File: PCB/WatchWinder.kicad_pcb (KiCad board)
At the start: 2 copper layers, 80 x 36.8 mm, 10 parts, among them J1 Screw_Terminal_01x02, J2 Screw_Terminal_01x02, J3 Screw_Terminal_01x12, J4 MOTOR, J5 Screw_Terminal_01x04

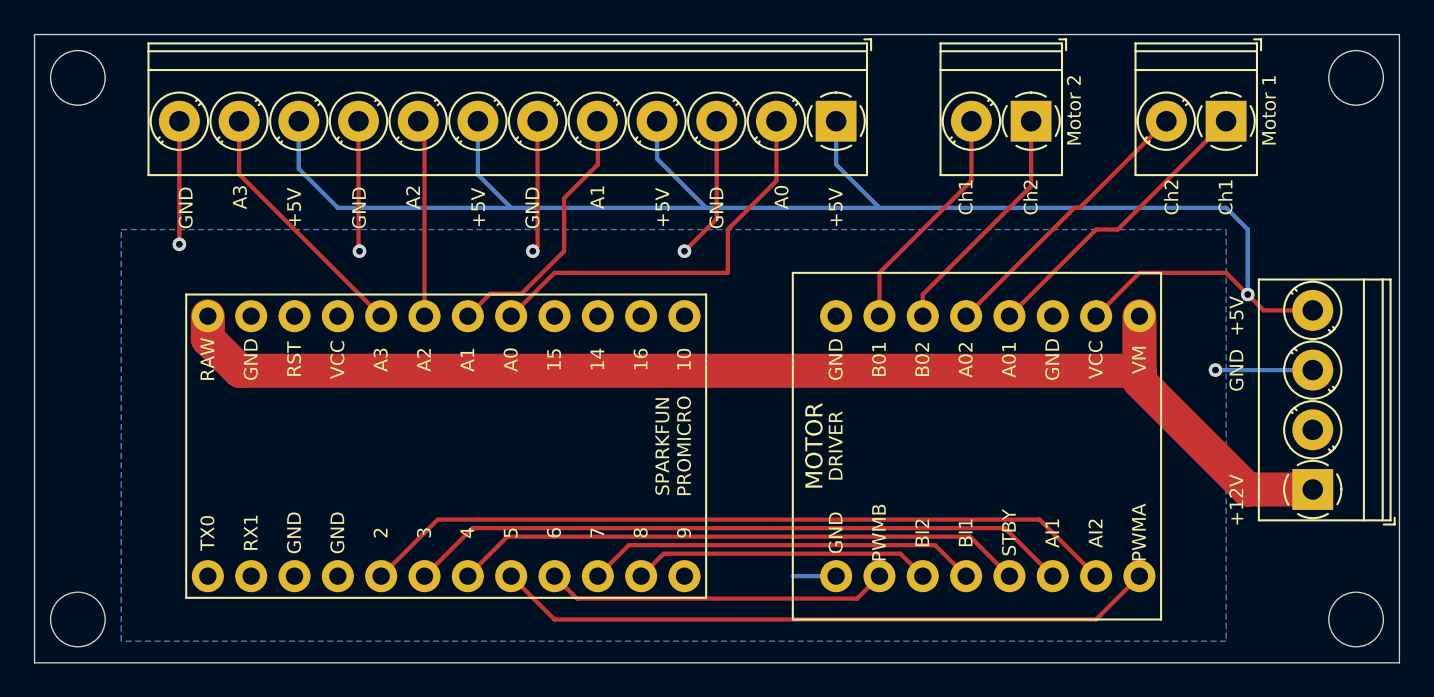
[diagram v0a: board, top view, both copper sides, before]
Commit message: Updated ground traces on PCB
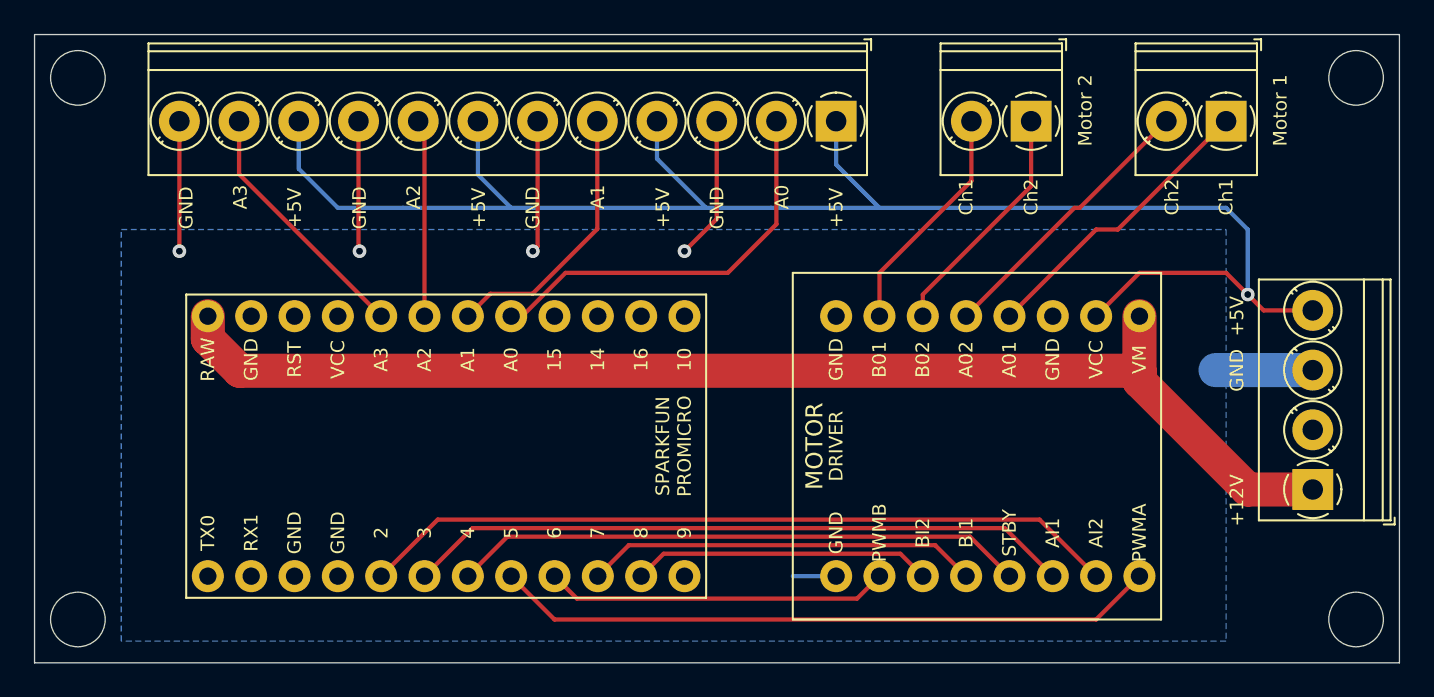
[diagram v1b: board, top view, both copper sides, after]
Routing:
- net GND: track 39.2 -> 39.6 mm, vias 5 -> 4
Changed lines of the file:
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@@
     (thickness 1.6)
     (drawings 29)
-    (tracks 93)
+    (tracks 91)
     (zones 0)
     (modules 10)
@@
   (setup
     (last_trace_width 0.25)
+    (user_trace_width 0.25)
+    (user_trace_width 2)
     (trace_clearance 0.25)
     (zone_clearance 0.508)
@@
     (effects (font (size 0.8 0.8) (thickness 0.15)))
   )
-  (gr_text "Motor 2" (at 135.89 76.835 90) (layer F.SilkS)
-    (effects (font (size 0.8 0.8) (thickness 0.15)))
-  )
-  (gr_text "Motor 1" (at 147.32 76.835 90) (layer F.SilkS)
+  (gr_text "Motor 2" (at 136.525 76.835 90) (layer F.SilkS)
+    (effects (font (size 0.8 0.8) (thickness 0.15)))
+  )
+  (gr_text "Motor 1" (at 147.955 76.835 90) (layer F.SilkS)
     (effects (font (size 0.8 0.8) (thickness 0.15)))
   )
@@
   (segment (start 149.86 99.06) (end 146.05 99.06) (width 2) (layer F.Cu) (net 1))
   (segment (start 121.92 104.14) (end 119.38 104.14) (width 0.25) (layer B.Cu) (net 2))
-  (segment (start 83.42 77.47) (end 83.42 84.69) (width 0.25) (layer F.Cu) (net 2))
-  (via (at 83.42 84.69) (size 0.8) (drill 0.4) (layers F.Cu B.Cu) (net 2))
   (via (at 93.98 85.09) (size 0.8) (drill 0.4) (layers F.Cu B.Cu) (net 2))
   (segment (start 93.92 85.03) (end 93.98 85.09) (width 0.25) (layer F.Cu) (net 2))
   (segment (start 93.92 77.47) (end 93.92 85.03) (width 0.25) (layer F.Cu) (net 2))
-  (via (at 104.14 85.09) (size 0.8) (drill 0.4) (layers F.Cu B.Cu) (net 2))
-  (segment (start 104.42 84.81) (end 104.14 85.09) (width 0.25) (layer F.Cu) (net 2))
-  (segment (start 104.42 77.47) (end 104.42 84.81) (width 0.25) (layer F.Cu) (net 2))
   (via (at 113.03 85.09) (size 0.8) (drill 0.4) (layers F.Cu B.Cu) (net 2))
   (segment (start 114.92 83.2) (end 113.03 85.09) (width 0.25) (layer F.Cu) (net 2))
   (segment (start 114.92 77.47) (end 114.92 83.2) (width 0.25) (layer F.Cu) (net 2))
-  (segment (start 149.86 92.06) (end 144.16 92.06) (width 0.25) (layer B.Cu) (net 2))
-  (via (at 144.16 92.06) (size 0.8) (drill 0.4) (layers F.Cu B.Cu) (net 2))
+  (segment (start 149.86 92.06) (end 144.16 92.06) (width 2) (layer B.Cu) (net 2))
+  (via (at 83.42 85.090026) (size 0.8) (drill 0.4) (layers F.Cu B.Cu) (net 2))
+  (segment (start 83.42 77.47) (end 83.42 85.090026) (width 0.25) (layer F.Cu) (net 2))
+  (segment (start 104.42 84.810022) (end 104.140022 85.09) (width 0.25) (layer F.Cu) (net 2))
+  (segment (start 104.42 77.47) (end 104.42 84.810022) (width 0.25) (layer F.Cu) (net 2))
+  (via (at 104.140022 85.09) (size 0.8) (drill 0.4) (layers F.Cu B.Cu) (net 2))
   (segment (start 86.92 80.57) (end 86.92 77.47) (width 0.25) (layer F.Cu) (net 5))
   (segment (start 95.25 88.9) (end 86.92 80.57) (width 0.25) (layer F.Cu) (net 5))
@@
   (segment (start 97.79 77.84) (end 97.42 77.47) (width 0.25) (layer F.Cu) (net 6))
   (segment (start 97.79 88.9) (end 97.79 77.84) (width 0.25) (layer F.Cu) (net 6))
-  (segment (start 107.95 80.01) (end 107.95 77.5) (width 0.25) (layer F.Cu) (net 7))
-  (segment (start 105.97288 81.98712) (end 107.95 80.01) (width 0.25) (layer F.Cu) (net 7))
-  (segment (start 105.97288 85.09) (end 105.97288 81.98712) (width 0.25) (layer F.Cu) (net 7))
-  (segment (start 107.95 77.5) (end 107.92 77.47) (width 0.25) (layer F.Cu) (net 7))
-  (segment (start 103.477681 87.585199) (end 105.97288 85.09) (width 0.25) (layer F.Cu) (net 7))
-  (segment (start 101.644801 87.585199) (end 103.477681 87.585199) (width 0.25) (layer F.Cu) (net 7))
+  (segment (start 107.92 79.167056) (end 107.92 77.47) (width 0.25) (layer F.Cu) (net 7))
+  (segment (start 101.644801 87.585199) (end 104.123303 87.585199) (width 0.25) (layer F.Cu) (net 7))
   (segment (start 100.33 88.9) (end 101.644801 87.585199) (width 0.25) (layer F.Cu) (net 7))
-  (segment (start 118.42 80.97) (end 118.42 77.47) (width 0.25) (layer F.Cu) (net 8))
-  (segment (start 115.57 86.36) (end 115.57 83.82) (width 0.25) (layer F.Cu) (net 8))
-  (segment (start 105.41 86.36) (end 115.57 86.36) (width 0.25) (layer F.Cu) (net 8))
-  (segment (start 115.57 83.82) (end 118.42 80.97) (width 0.25) (layer F.Cu) (net 8))
-  (segment (start 102.87 88.9) (end 105.41 86.36) (width 0.25) (layer F.Cu) (net 8))
+  (segment (start 104.123303 87.585199) (end 107.92 83.788502) (width 0.25) (layer F.Cu) (net 7))
+  (segment (start 107.92 83.788502) (end 107.92 79.167056) (width 0.25) (layer F.Cu) (net 7))
+  (segment (start 103.515624 88.9) (end 106.055624 86.36) (width 0.25) (layer F.Cu) (net 8))
+  (segment (start 118.42 79.167056) (end 118.42 77.47) (width 0.25) (layer F.Cu) (net 8))
+  (segment (start 102.87 88.9) (end 103.515624 88.9) (width 0.25) (layer F.Cu) (net 8))
+  (segment (start 106.055624 86.36) (end 115.57 86.36) (width 0.25) (layer F.Cu) (net 8))
+  (segment (start 115.57 86.36) (end 118.42 83.51) (width 0.25) (layer F.Cu) (net 8))
+  (segment (start 118.42 83.51) (end 118.42 79.167056) (width 0.25) (layer F.Cu) (net 8))
   (segment (start 125.685199 102.825199) (end 127 104.14) (width 0.25) (layer F.Cu) (net 14))
   (segment (start 111.804801 102.825199) (end 125.685199 102.825199) (width 0.25) (layer F.Cu) (net 14))
@@
   (segment (start 121.92 77.47) (end 121.92 80.01) (width 0.25) (layer B.Cu) (net 29))
   (segment (start 121.92 80.01) (end 124.46 82.55) (width 0.25) (layer B.Cu) (net 29))
-  (segment (start 111.42 77.47) (end 111.42 79.67) (width 0.25) (layer B.Cu) (net 29))
-  (segment (start 111.42 79.67) (end 114.3 82.55) (width 0.25) (layer B.Cu) (net 29))
   (segment (start 114.3 82.55) (end 118.11 82.55) (width 0.25) (layer B.Cu) (net 29))
   (segment (start 107.95 82.55) (end 114.3 82.55) (width 0.25) (layer B.Cu) (net 29))
   (segment (start 100.92 80.6) (end 102.87 82.55) (width 0.25) (layer B.Cu) (net 29))
   (segment (start 100.92 77.47) (end 100.92 80.6) (width 0.25) (layer B.Cu) (net 29))
-  (segment (start 102.87 82.55) (end 96.52 82.55) (width 0.25) (layer B.Cu) (net 29))
   (segment (start 107.95 82.55) (end 102.87 82.55) (width 0.25) (layer B.Cu) (net 29))
-  (segment (start 90.42 80.26) (end 92.71 82.55) (width 0.25) (layer B.Cu) (net 29))
-  (segment (start 90.42 77.47) (end 90.42 80.26) (width 0.25) (layer B.Cu) (net 29))
-  (segment (start 96.52 82.55) (end 92.71 82.55) (width 0.25) (layer B.Cu) (net 29))
   (segment (start 149.86 88.56) (end 146.98 88.56) (width 0.25) (layer F.Cu) (net 29))
-  (via (at 146.05 87.63) (size 0.8) (drill 0.4) (layers F.Cu B.Cu) (net 29) (status 1000000))
+  (via (at 146.05 87.63) (size 0.8) (drill 0.4) (layers F.Cu B.Cu) (net 29))
   (segment (start 146.98 88.56) (end 146.05 87.63) (width 0.25) (layer F.Cu) (net 29))
   (segment (start 146.05 87.63) (end 146.05 83.82) (width 0.25) (layer B.Cu) (net 29))
@@
   (segment (start 139.7 86.36) (end 144.78 86.36) (width 0.25) (layer F.Cu) (net 29))
   (segment (start 137.16 88.9) (end 139.7 86.36) (width 0.25) (layer F.Cu) (net 29))
+  (segment (start 96.52 82.55) (end 102.87 82.55) (width 0.25) (layer B.Cu) (net 29))
+  (segment (start 92.71 82.55) (end 96.52 82.55) (width 0.25) (layer B.Cu) (net 29))
+  (segment (start 90.42 80.26) (end 92.71 82.55) (width 0.25) (layer B.Cu) (net 29))
+  (segment (start 90.42 77.47) (end 90.42 80.26) (width 0.25) (layer B.Cu) (net 29))
+  (segment (start 111.42 79.67) (end 114.3 82.55) (width 0.25) (layer B.Cu) (net 29))
+  (segment (start 111.42 77.47) (end 111.42 79.67) (width 0.25) (layer B.Cu) (net 29))
   (zone (net 2) (net_name GND) (layer B.Cu) (hatch edge 0.508)
     (connect_pads (clearance 0.508))
